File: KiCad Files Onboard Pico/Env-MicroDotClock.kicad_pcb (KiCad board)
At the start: 2 copper layers, 110 x 80 mm, 102 parts, among them IC1 IS31FL3730-QFLS2-TR, IC2 IS31FL3730-QFLS2-TR, IC3 IS31FL3730-QFLS2-TR, IC4 IS31FL3730-QFLS2-TR, J1 Conn_01x06_Pin, J3 Button, M1 Dip-14 Socket, M2 Dip-14 Socket, M3 Dip-14 Socket, M4 Dip-14 Socket, M5 Dip-14 Socket, M6 Dip-14 Socket, M7 Dip-14 Socket, M8 Dip-14 Socket, Q1 2SC1815, SW1 SW_Push, SW2 SW_Push, SW3 SW_Push, SW4 SW_Push, SW5 SW_Push, U1 Si7021-A20, U2 SOT-23-5 5.5V 3.3V 500mA, U3 DS3231M, U4 RP2040, Y1 3225_4P 12MHz

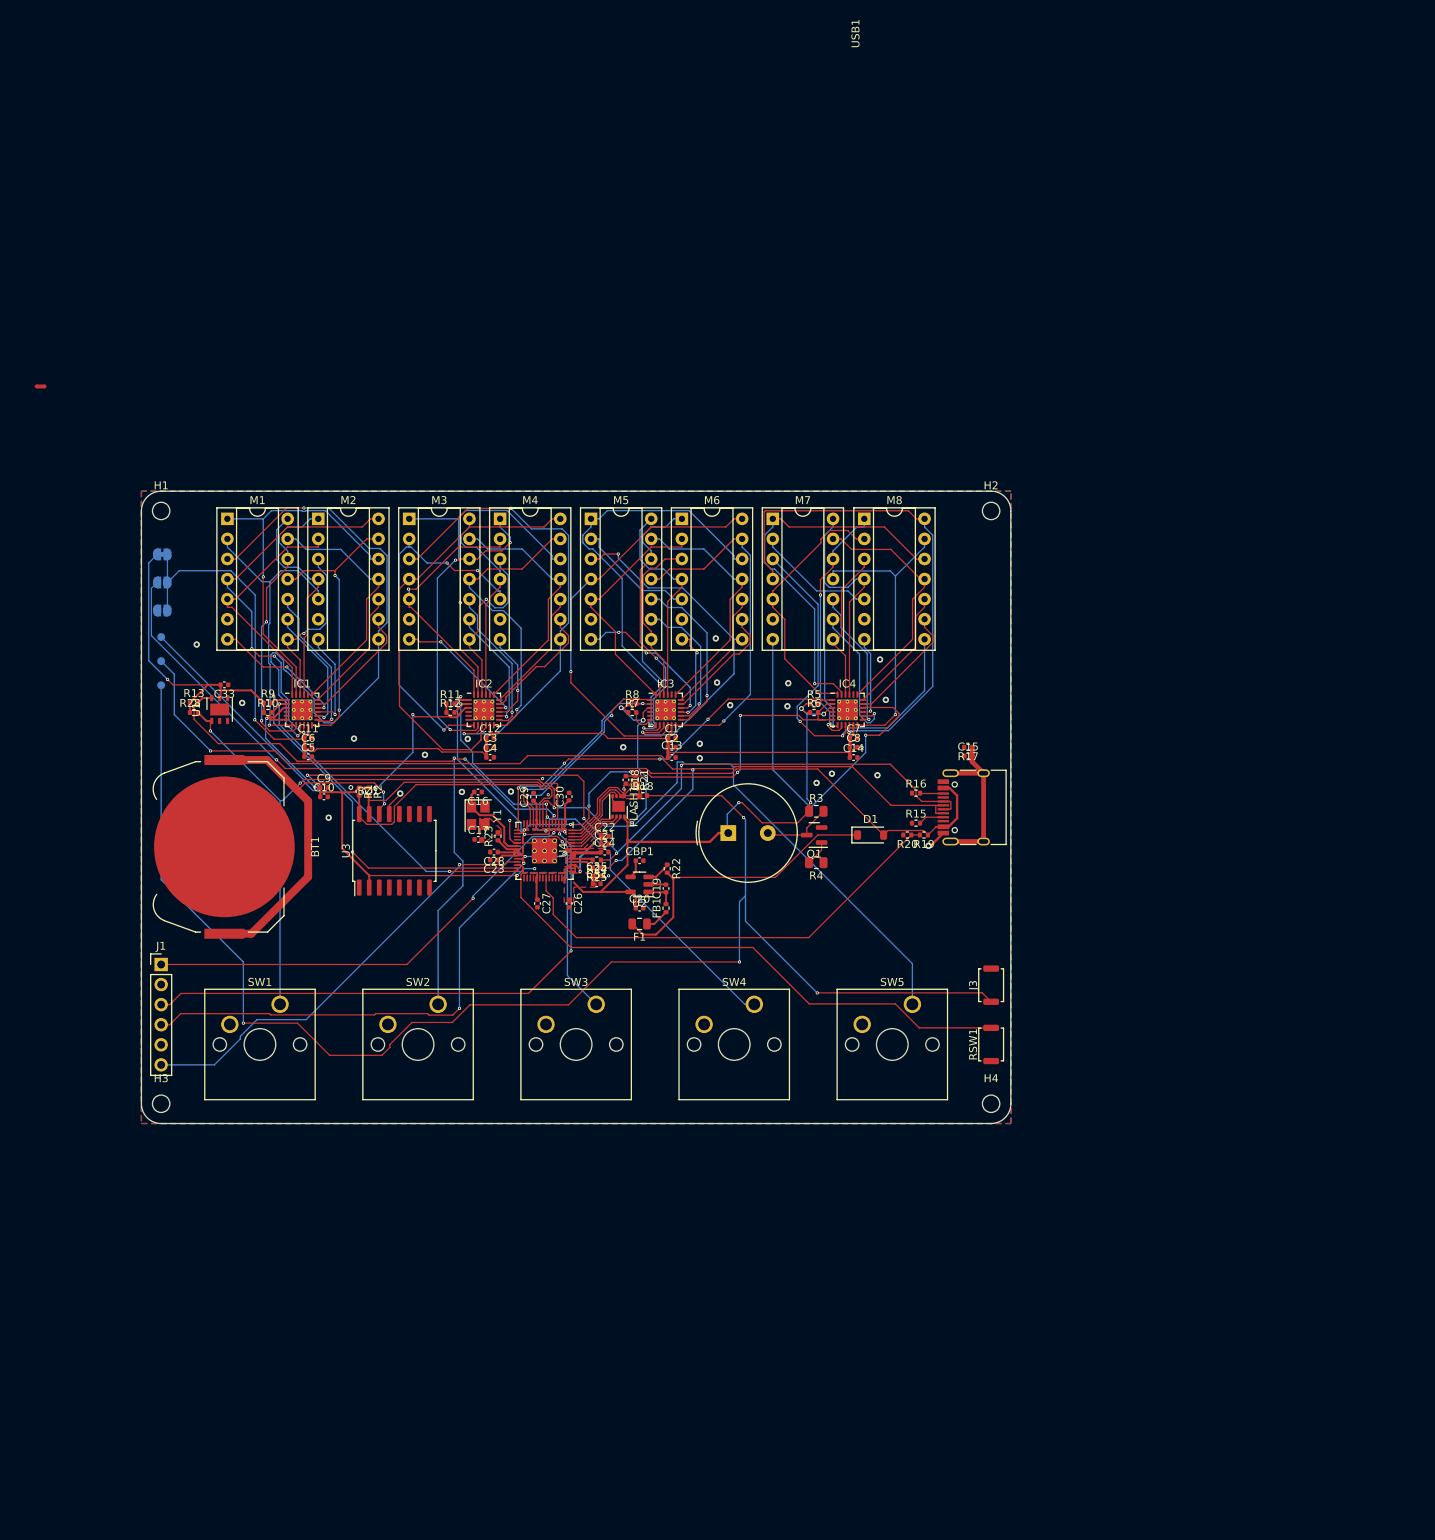
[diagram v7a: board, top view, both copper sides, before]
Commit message: began rework of onboard 2040 pcb
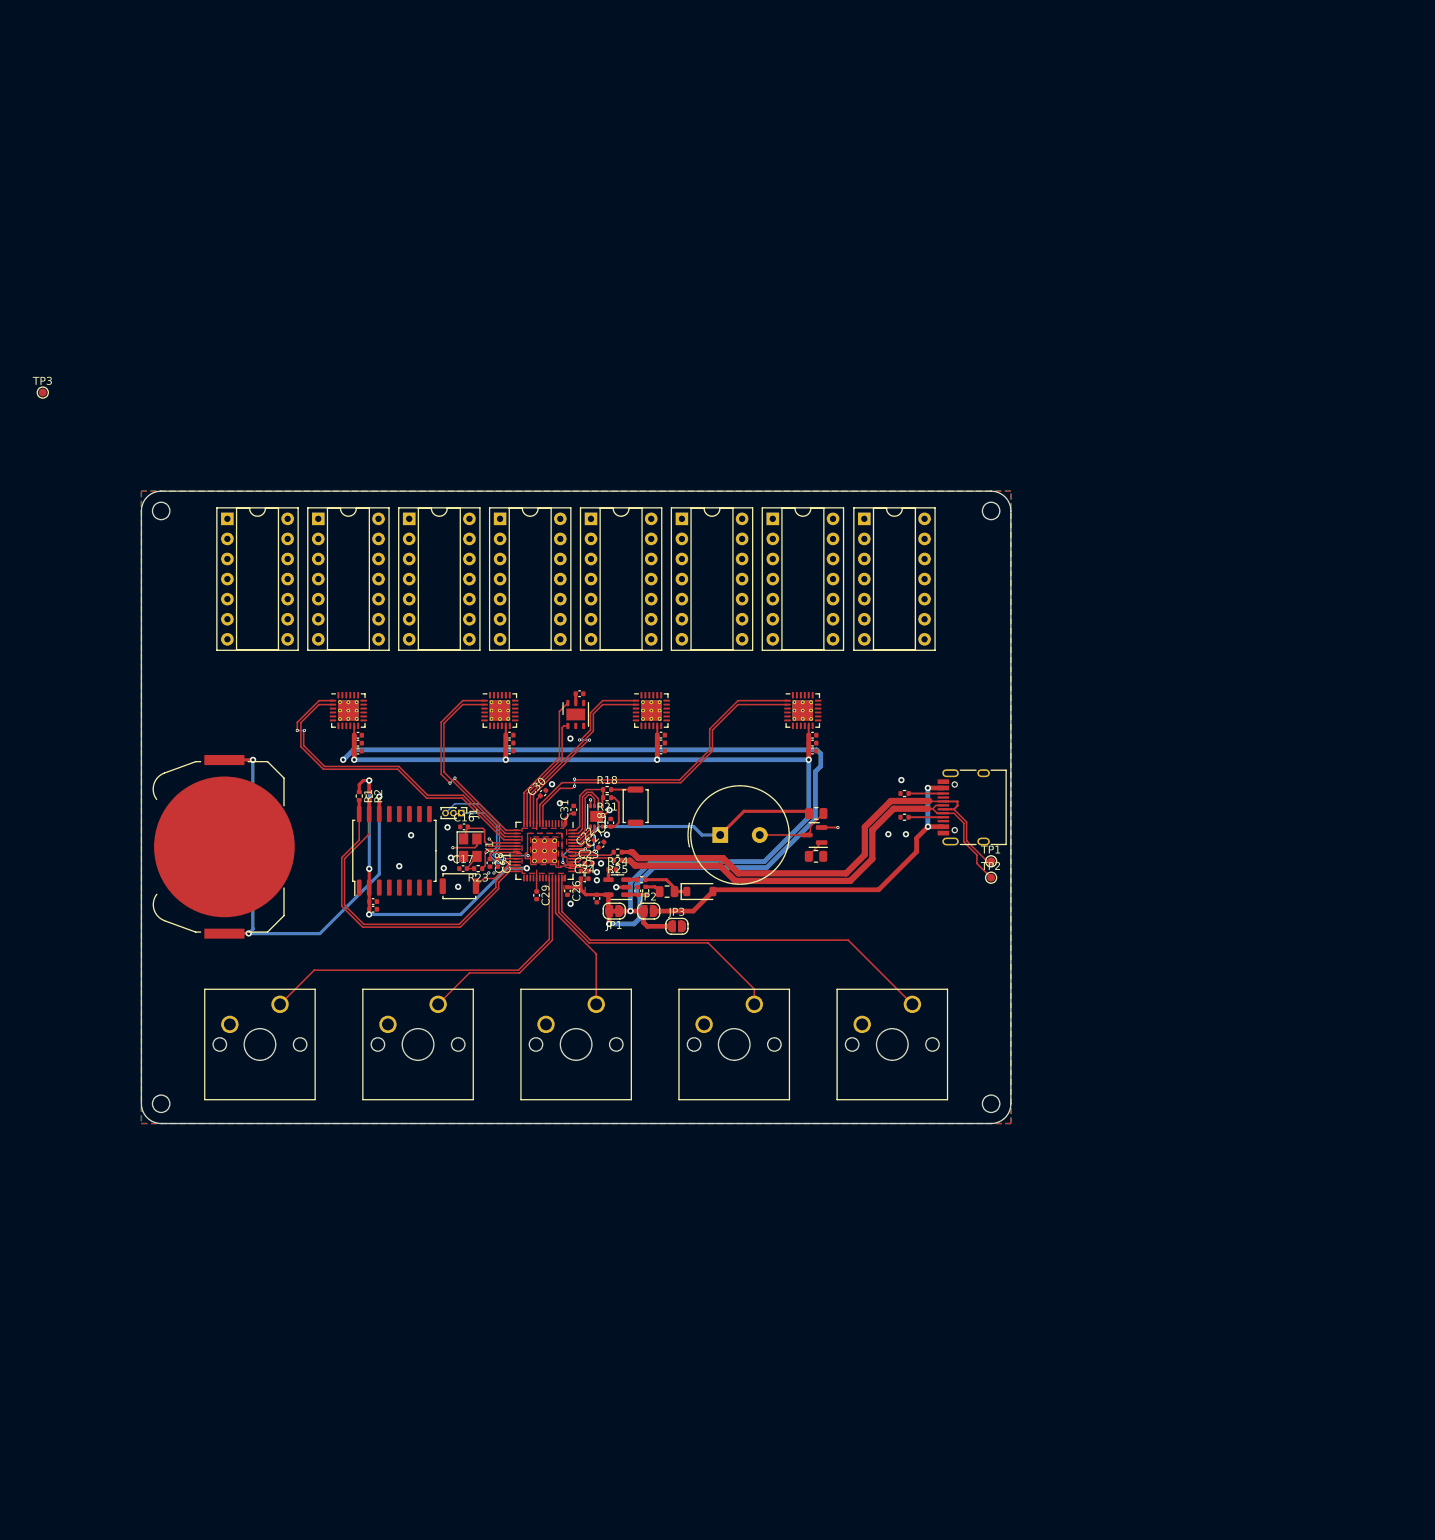
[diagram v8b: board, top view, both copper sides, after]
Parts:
- removed C15: 0.1uf 0402, Capacitor_SMD:C_0402_1005Metric
- removed NT1: NetTie_2, NetTie:NetTie-2_SMD_Pad0.5mm
- removed R10, R11, R12, R13, R28, R5, R6, R7, R8, R9: 0402 10K, Resistor_SMD:R_0402_1005Metric
- removed R17: 220 0402, Resistor_SMD:R_0402_1005Metric
- removed R19: 5.6K 0402, Resistor_SMD:R_0402_1005Metric
- removed R20: 10K 0402, Resistor_SMD:R_0402_1005Metric
- J1: value Conn_01x06_Pin -> Conn_01x03; footprint Connector_PinHeader_2.54mm:PinHeader_1x06_P2.54mm_Vertical -> Connector_PinHeader_1.00mm:PinHeader_1x03_P1.00mm_Vertical
- JP1, JP2, JP3, TP1, TP2, TP3: moved to F.Cu
- moved TP1 108.8 mm to (121.0, 60.3), turned to 0 degrees
- moved TP2 108.5 mm to (121.0, 62.4), turned to 0 degrees
- moved JP3 76.4 mm to (81.2, 68.5), turned to 0 degrees
- moved JP2 74.3 mm to (77.7, 66.6), turned to 0 degrees
- moved JP1 72.8 mm to (73.3, 66.6)
- moved RSW1 70.2 mm to (53.7, 63.5), turned to 0 degrees
- moved J3 50.4 mm to (76.0, 53.4), turned to -90 degrees
- moved U1 45.1 mm to (68.5, 41.8)
- moved C33 44.9 mm to (68.9, 39.1)
- moved J1 42.5 mm to (54.0, 54.2), turned to -90 degrees
- moved TP3 39.9 mm to (1.02, 1.02), turned to 0 degrees
- moved D1 22.8 mm to (84.2, 64.2)
- moved C9 15.7 mm to (42.8, 65.4)
- moved C10 15.5 mm to (42.8, 66.4)
- moved C21 13.8 mm to (58.6, 60.5), turned to -90 degrees
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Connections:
- BT1 pad 2: DEBUG-GND -> GND
- C1 pad 2: DEBUG-GND -> GND
- C10 pad 2: DEBUG-GND -> GND
- C11 pad 2: DEBUG-GND -> GND
- C12 pad 2: DEBUG-GND -> GND
- C13 pad 2: DEBUG-GND -> GND
- C14 pad 2: DEBUG-GND -> GND
- C16 pad 1: DEBUG-GND -> GND
- C17 pad 1: DEBUG-GND -> GND
- C18 pad 2: DEBUG-GND -> GND
- C19 pad 2: DEBUG-GND -> GND
- C2 pad 2: DEBUG-GND -> GND
- C20 pad 2: DEBUG-GND -> GND
- C21 pad 2: DEBUG-GND -> GND
- C22 pad 2: DEBUG-GND -> GND
- C23 pad 2: DEBUG-GND -> GND
- C24 pad 2: DEBUG-GND -> GND
- C25 pad 2: DEBUG-GND -> GND
- C26 pad 2: DEBUG-GND -> GND
- C27 pad 2: DEBUG-GND -> GND
- C28 pad 2: DEBUG-GND -> GND
- C29 pad 2: DEBUG-GND -> GND
- C3 pad 2: DEBUG-GND -> GND
- C30 pad 2: DEBUG-GND -> GND
- C31 pad 2: DEBUG-GND -> GND
- C33 pad 1: DEBUG-GND -> GND
- C4 pad 2: DEBUG-GND -> GND
- C5 pad 2: DEBUG-GND -> GND
- C6 pad 2: DEBUG-GND -> GND
- C7 pad 2: DEBUG-GND -> GND
- C8 pad 2: DEBUG-GND -> GND
- C9 pad 2: DEBUG-GND -> GND
- CBP1 pad 2: DEBUG-GND -> GND
- FLASH1 pad 4: DEBUG-GND -> GND
- FLASH1 pad 9: DEBUG-GND -> GND
- IC1 pad 1: GPIO16 -> GPIO14
- IC1 pad 2: GPIO17 -> GPIO15
- IC1 pad 20: DEBUG-GND -> GND
- IC1 pad 25: DEBUG-GND -> GND
- IC2 pad 1: GPIO4 -> GPIO12
- IC2 pad 2: GPIO5 -> GPIO13
- IC2 pad 20: DEBUG-GND -> GND
- IC2 pad 25: DEBUG-GND -> GND
- IC2 pad 6: DEBUG-GND -> GND
- IC3 pad 20: DEBUG-GND -> GND
- IC3 pad 25: DEBUG-GND -> GND
- IC4 pad 1: GPIO12 -> GPIO6
- IC4 pad 2: GPIO13 -> GPIO7
- IC4 pad 20: DEBUG-GND -> GND
- IC4 pad 25: DEBUG-GND -> GND
- IC4 pad 6: GPIO13 -> GPIO7
- J1 pad 1: GPIO1 -> SWDIO
- J1 pad 2: DEBUG-GND -> GND
- J1 pad 3: GPIO0 -> SWCLK
- J3 pad 2: DEBUG-GND -> GND
- Q1 pad 2: DEBUG-GND -> GND
- R1 pad 2: GPIO7 -> GPIO17
- R15 pad 1: DEBUG-GND -> GND
- R16 pad 1: DEBUG-GND -> GND
- R2 pad 2: GPIO6 -> GPIO16
- RSW1 pad 1: DEBUG-GND -> GND
- SW1 pad 1: GPIO2 -> GPIO25
- SW1 pad 2: DEBUG-GND -> GND
- SW2 pad 1: GPIO3 -> ADC0
- SW2 pad 2: DEBUG-GND -> GND
- SW3 pad 1: GPIO4 -> ADC1
- SW3 pad 2: DEBUG-GND -> GND
- SW4 pad 1: GPIO5 -> ADC2
- SW4 pad 2: DEBUG-GND -> GND
- SW5 pad 1: GPIO6 -> ADC3
- SW5 pad 2: DEBUG-GND -> GND
- U1 pad 1: GPIO2 -> GPIO10
- U1 pad 2: DEBUG-GND -> GND
- U1 pad 6: GPIO3 -> GPIO11
- U2 pad 2: DEBUG-GND -> GND
- U3 pad 10: DEBUG-GND -> GND
- U3 pad 11: DEBUG-GND -> GND
- U3 pad 12: DEBUG-GND -> GND
- U3 pad 13: DEBUG-GND -> GND
- U3 pad 15: GPIO6 -> GPIO16
- U3 pad 16: GPIO7 -> GPIO17
- U3 pad 5: DEBUG-GND -> GND
- U3 pad 6: DEBUG-GND -> GND
- U3 pad 7: DEBUG-GND -> GND
- U3 pad 8: DEBUG-GND -> GND
- U3 pad 9: DEBUG-GND -> GND
- U4 pad 19: DEBUG-GND -> GND
- U4 pad 57: DEBUG-GND -> GND
- USB1 pad 1: DEBUG-GND -> GND
- USB1 pad 12: DEBUG-GND -> GND
- USB1 pad 13: Net-(USB1-SHIELD) -> GND
- Y1 pad 2: DEBUG-GND -> GND
- Y1 pad 4: DEBUG-GND -> GND
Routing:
- net /Onboard Pico/~{USB_BOOT}: track 187.2 -> 3.09 mm, vias 4 -> 0
- net GPIO3: track 89.2 -> 0.00 mm, vias 3 -> 0
- net GPIO2: track 83.3 -> 0.00 mm, vias 2 -> 0
- net VBUS: track 126.3 -> 48.9 mm, vias 1 -> 2
- net IC1R3: track 75.8 -> 0.00 mm, vias 2 -> 0
- net GPIO0: track 71.5 -> 0.00 mm, vias 2 -> 0
- net USB_D+: track 131.8 -> 60.8 mm, vias 4 -> 0
- net USB_D-: track 131.0 -> 60.9 mm, vias 3 -> 0
- net IC4R4: track 65.3 -> 0.00 mm, vias 1 -> 0
- net /Onboard Pico/RUN: track 71.1 -> 6.35 mm
- net GPIO5: track 62.1 -> 0.00 mm, vias 3 -> 0
- net GPIO6: track 102.3 -> 40.9 mm, vias 1 -> 2
- net IC2R3: track 60.1 -> 0.00 mm, vias 2 -> 0
- net GPIO1: track 58.2 -> 0.00 mm, vias 2 -> 0
- net GPIO24: track 58.0 -> 0.00 mm
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- added copper zone on B.Cu, net GND
- added copper zone on F.Cu, net GND
- removed copper zone on B.Cu, net +3V3
- removed copper zone on F.Cu, net /Onboard Pico/QSPI_SS
- removed copper zone on B.Cu, net DEBUG-GND
- removed copper zone on F.Cu, net DEBUG-GND
- removed copper zone on F.Cu, net Net-(C17-Pad2)
